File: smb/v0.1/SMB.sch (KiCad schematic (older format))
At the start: 26 parts, among them IC101 ATMEGA1284-A, J102 RTS_RESET, J103 ICSP, J104 SERIAL_REV, P101 I2C_CONN, P102 CONN_6, P104 CONN_5X2, P105 CONN_7, SW101 SKQGAKE010, X101 20MHz

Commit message: modif schema
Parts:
- removed P102: CONN_6, symbol CONN_6
- added D102: LED, LED-0603, symbol LED
- added J101: RJ45, ~, symbol RJ45
- added P106: CONN_7, symbol CONN_5X2
- added P107: CONN_7, symbol CONN_3X2
- added R1: 3.3kR, SM0603, symbol R
- P105: symbol CONN_7 -> CONN_8
- gave numbers to parts that had none: 1
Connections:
- net labels added: LED_STATUS, PA0, PA1, PA2, PA3, PA4, PA5, PA6, PA7, PB0, PC2, PC3, PC4, PC5, PC6, PC7, PD4, PD5, RX0, RX1, TX0, TX1, clock
- net labels removed: ADC[0..7], RX, TX
- wire segments 133 -> 150
- no-connect marks 0 -> 5
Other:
- note added: "Front Panel connector\n1- 5V\n2- 3,3V\n3- Tx0\n4- Rx0\n5- Status\n6- \n7- Reset\n8- GND"
- note added: "I/O extension #1"
- note added: "I/O extension #2"
- note added: "I2C connector\nto external boards"
- note added: "I2C connector\nto internal boards"
- note added: "TinyRTC slot"
- note added: "UART connector"
- note added: "j'ai harmonisé les tailles\ndes connecteurs:\n2x5 avec 5V sur 1 et GND sur 2"
- note added: "pour extension RS485 par exemple.\nJ'ai ajouté 2 I/O pour pilotage du max485"
- note removed: "Connecteur pour \nTinyRTC"
- note removed: "Connecteur pour carte ext :\n1- 5V\n2- 3,3V\n3- GND\n4- Rx0\n5- Tx0\n6- Reset\n7- Status\n8-"
- moved on the sheet: C107, D101, GS1, J102, J103, J104, P101, R102, R104, R105, R106, SW101

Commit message: Add slot I2C
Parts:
- added P108: CONN_7, symbol CONN_8
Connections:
- wire segments 150 -> 156
- no-connect marks 5 -> 9
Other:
- note added: "I2C slot"
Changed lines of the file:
@@
-EESchema Schematic File Version 2  date mar. 14 mai 2013 12:19:51 CEST
+EESchema Schematic File Version 2  date mar. 14 mai 2013 13:16:05 CEST
 LIBS:power
 LIBS:device
@@
 Text Notes 9900 3100 0    60   ~ 0
 I2C connector\nto internal boards
+$Comp
+L CONN_8 P108
+U 1 1 51921C93
+P 7500 950
+F 0 "P108" V 7470 950 60  0000 C CNN
+F 1 "CONN_7" V 7570 950 60  0000 C CNN
+F 2 "" H 7500 950 60  0001 C CNN
+F 3 "" H 7500 950 60  0001 C CNN
+	1    7500 950
+	0    -1   -1   0
+$EndComp
+$Comp
+L GND #PWR?
+U 1 1 51921C99
+P 7250 1450
+F 0 "#PWR?" H 7250 1450 30  0001 C CNN
+F 1 "GND" H 7250 1380 30  0001 C CNN
+F 2 "" H 7250 1450 60  0001 C CNN
+F 3 "" H 7250 1450 60  0001 C CNN
+	1    7250 1450
+	1    0    0    -1
+$EndComp
+$Comp
+L +5V #PWR?
+U 1 1 51921C9F
+P 6950 1300
+F 0 "#PWR?" H 6950 1390 20  0001 C CNN
+F 1 "+5V" H 6950 1390 30  0000 C CNN
+F 2 "" H 6950 1300 60  0001 C CNN
+F 3 "" H 6950 1300 60  0001 C CNN
+	1    6950 1300
+	1    0    0    -1
+$EndComp
+Text GLabel 7550 1400 3    25   BiDi ~ 0
+SCL
+Text GLabel 7450 1400 3    25   BiDi ~ 0
+SDA
+Text Notes 7150 750  0    60   ~ 0
+I2C slot
+Text GLabel 7850 1450 3    25   BiDi ~ 0
+clock
+Wire Wire Line
+	7250 1300 7250 1450
+Wire Wire Line
+	6950 1300 6950 1550
+Wire Wire Line
+	6950 1550 7350 1550
+Wire Wire Line
+	7350 1550 7350 1300
+Wire Wire Line
+	7450 1400 7450 1300
+Wire Wire Line
+	7550 1300 7550 1400
+NoConn ~ 7850 1300
+NoConn ~ 7750 1300
+NoConn ~ 7650 1300
+NoConn ~ 7150 1300
+Wire Notes Line
+	6800 600  6800 1700
+Wire Notes Line
+	6800 1700 8000 1700
+Wire Notes Line
+	8000 1700 8000 600
+Wire Notes Line
+	8000 600  6800 600
 $EndSCHEMATC

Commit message: SMBV0.1 Mise ? jour Slot TinyRTC + I2C Slot
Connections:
- net labels added: Bat, DS
- wire segments 156 -> 172
- no-connect marks 9 -> 1

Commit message: Mise ? jour de la SMBV0.1
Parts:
- removed P102: CONN_4X2, symbol CONN_4X2
- removed P105, P108: CONN_7, symbol CONN_8
- added P102: CONN_5X2, ~, symbol CONN_5X2
- added P105, P108: CONN_5, ~, symbol CONN_5
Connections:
- net labels removed: Bat, PB0, clock
- wire segments 172 -> 165
- no-connect marks 1 -> 0
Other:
- note added: "1-Wire I2C Slot\n"
- note added: "Front Panel connector\n1- 5V\n2- 3,3V\n3- Tx0\n4- Rx0\n5- LED_Status\n6- /RESET\n7- PA6\n8- PA7\n9- \n10- GND"
- note added: "Front Panel\n"
- note added: "UART Connector"
- note removed: "Front Panel connector\n1- 5V\n2- 3,3V\n3- Tx0\n4- Rx0\n5- Status\n6- \n7- Reset\n8- GND"
- moved on the sheet: J103

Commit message: SMB V0.1 Update
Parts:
- removed P102: CONN_5X2, ~, symbol CONN_5X2
- removed P104: CONN_5X2, symbol CONN_5X2
- removed P106: CONN_7, symbol CONN_5X2
- added P102, P103, P104, P106: CONN_3X2, symbol CONN_3X2
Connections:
- wire segments 165 -> 166
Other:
- note added: "2 I/O for Max485 driving"
- note added: "????"
- note added: "Extension"
- note added: "Front Panel Connector"
- note added: "I/O extension"
- note added: "I2C Connector"
- note added: "I2C SLOT"
- note added: "I2C Slot"
- note added: "Indications Lights"
- note added: "P102 : Basic Extension\nP103 : LCD Screen\nP104 : Button"
- note added: "PROG"
- note added: "Power"
- note added: "Prog with UART"
- note added: "Status"
- note removed: "Front Panel connector\n1- 5V\n2- 3,3V\n3- Tx0\n4- Rx0\n5- LED_Status\n6- /RESET\n7- PA6\n8- PA7\n9- \n10- GND"
- note removed: "Front Panel\n"
- note removed: "I/O extension #1"
- note removed: "I/O extension #2"
- note removed: "j'ai harmonisé les tailles\ndes connecteurs:\n2x5 avec 5V sur 1 et GND sur 2"
- note removed: "pour extension RS485 par exemple.\nJ'ai ajouté 2 I/O pour pilotage du max485"
- moved on the sheet: C101, C102, C103, C104, C105, C106, C107, D101, D102, GS1, IC101, J101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

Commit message: Draft PCB SMBV0.1
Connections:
- net GND: now also J101.9 (SHIELD)

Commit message: routage complet ajout rs485 attention, tous les packages sont ? v?rifier
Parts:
- removed P107: CONN_7, symbol CONN_3X2
- added GS2, GS3: GS2, symbol GS2
- added IC1: SP3485CN, SO8, symbol SP3485CN
- added P107: CONN_3, symbol CONN_5
- added R2, R3, R4: R, symbol R
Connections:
- net PD4 is gone; now on net LED_STATUS: IC101.13 ((PCINT28/XCK1/OC1B)PD4)
- net PD5 is gone; now on an unnamed net: IC101.14 ((PCINT294/OC1A)PD5)
- net +5V: now also IC1.7 (VCC), R3.2
- net DS: now also IC101.24 ((PCINT21/TDI)PC5); no longer IC101.40 ((PCINT8/T0/XCK)PB0)
- net GND: now also IC1.5 (GND), P107.1, R4.2
- net LED_STATUS: now also P102.2; no longer IC101.15 ((PCINT30/OC2B/ICP)PD6), P102.5
- net PC2: now also P106.3; no longer P106.2
- net PC3: now also P106.4; no longer P106.3
- net PC4: now also P106.2; no longer P106.4
- net RX0: now also P102.5; no longer P102.2
- net RX1: now also IC1.1 (RO)
- net TX1: now also IC1.4 (DI)
- net at GS1.2 (G2): no longer IC101.41 ((PCINT9/CLKO/T1)PB1)
- net PC5 renamed PD6
- net PD6: now also IC101.15 ((PCINT30/OC2B/ICP)PD6); no longer IC101.24 ((PCINT21/TDI)PC5)
- new net: P107.5, R2.2
- new net: GS2.2 (G2), R3.1
- new net: GS3.2 (G2), R4.1
- new net PB0: IC1.2 (~RE~), IC1.3 (DE), IC101.40 ((PCINT8/T0/XCK)PB0)
- new net TX+: GS2.1 (G1), IC1.6 (A), P107.2, P107.4
- new net TX-: GS3.1 (G1), IC1.7 (VCC), P107.3, R2.1
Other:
- note added: "Max485 driving"
- note removed: "2 I/O for Max485 driving"
- moved on the sheet: GS1

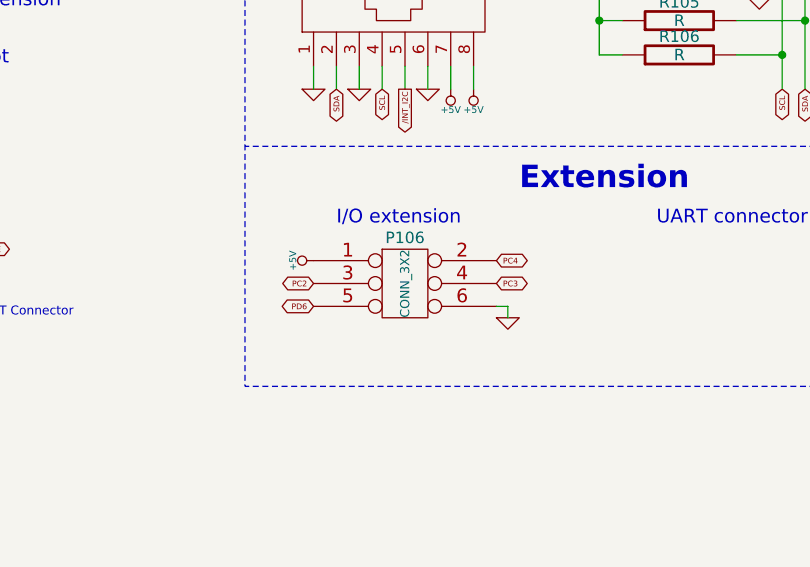
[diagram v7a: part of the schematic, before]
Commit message: routage, reprise plan de masse, suppression de vias
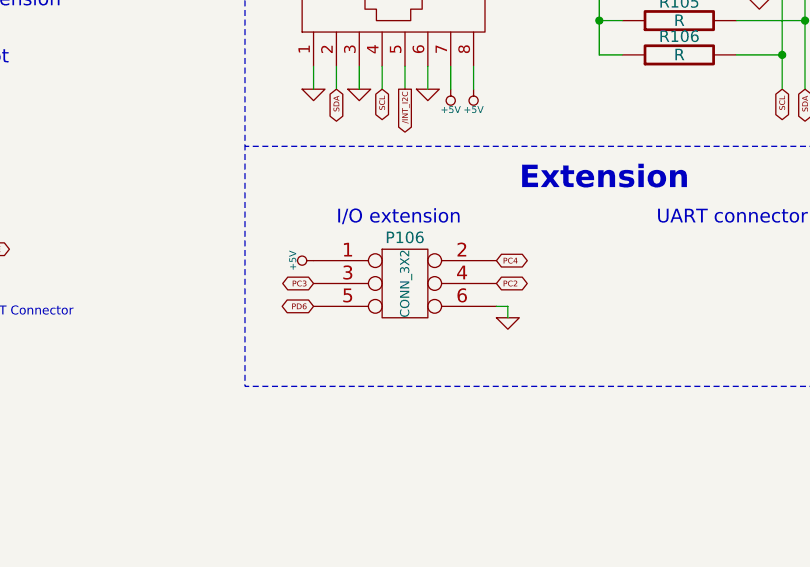
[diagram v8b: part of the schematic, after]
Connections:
- net PC2: now also P106.4; no longer P106.3
- net PC3: now also P106.3; no longer P106.4
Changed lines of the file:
@@
-EESchema Schematic File Version 2  date mer. 22 mai 2013 21:15:44 CEST
+EESchema Schematic File Version 2  date jeu. 23 mai 2013 13:21:39 CEST
 LIBS:power
 LIBS:device
@@
 Sheet 1 4
 Title "Short Main Board - SMB controller"
-Date "22 may 2013"
+Date "23 may 2013"
 Rev "0"
 Comp "XPLDUINO project"
@@
 PC4
 Text GLabel 8400 5800 0    25   BiDi ~ 0
+PC3
+Text GLabel 9200 5800 2    25   BiDi ~ 0
 PC2
-Text GLabel 9200 5800 2    25   BiDi ~ 0
-PC3
 Text GLabel 8400 5900 0    25   BiDi ~ 0
 PD6
